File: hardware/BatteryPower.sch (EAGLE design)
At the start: 36 parts, among them U1 CH004-2032LF, U2 ACS711ELCTR-12AB-T, U3 ACS711ELCTR-12AB-T

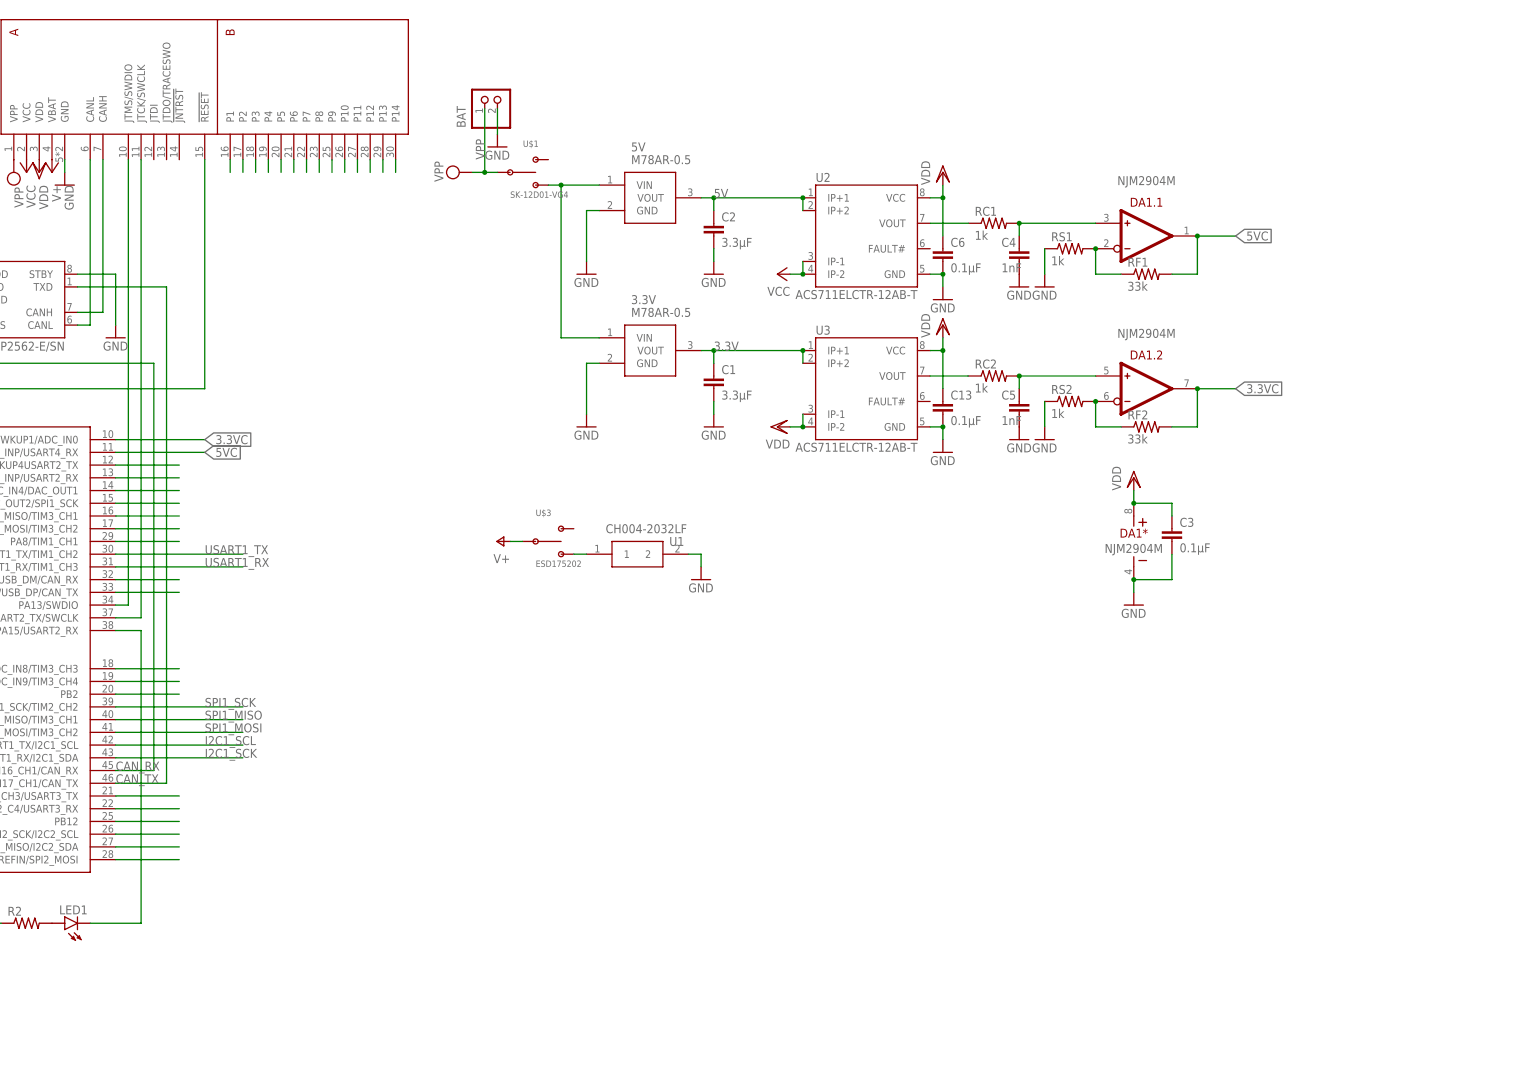
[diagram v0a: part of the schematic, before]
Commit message: Layout battery power board
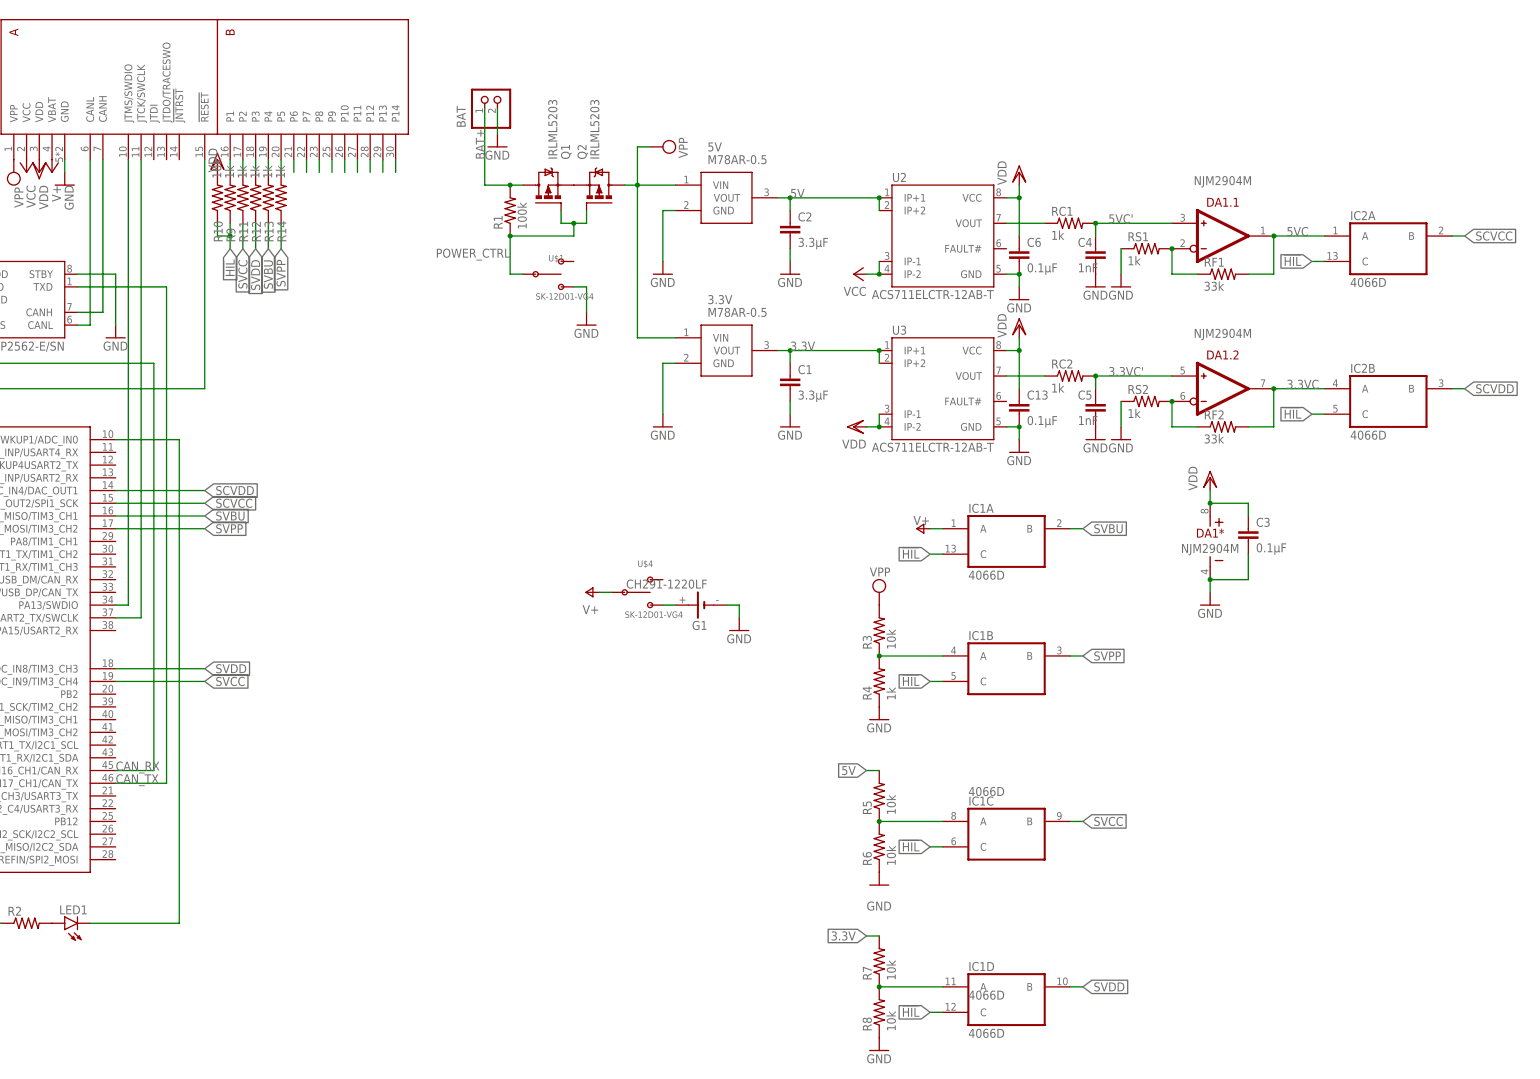
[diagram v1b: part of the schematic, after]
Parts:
- removed U$3: ESD175202, switches:ESD175202
- removed U1: CH004-2032LF, CH004-2032LF:CH004-2032LF
- added G1: CH291-1220LF, battery:CH291-1220LF
- added IC1, IC2: 4066D, 40xx:4066D
- added Q1, Q2: IRLML5203, transistor-power:IRLML5203
- added R1: 100k, rcl:R-US_R0603
- added R10, R3, R5, R6, R7, R8: 10k, rcl:R-US_R0603
- added R11, R12, R13, R14, R4, R9: 1k, rcl:R-US_R0603
- added U$4: SK-12D01-VG4, switches:SK-12D01-VG4
- BAT: device jst-ph:S2B-PH-K-S -> con-jst-xh:S2B-XH-A
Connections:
- net N$2 renamed 5VC'
- net N$3 renamed 3.3VC'
- removed net I2C1_SCK: STM32F001.PB7/USART1_RX/I2C1_SDA
- removed net I2C1_SCL: STM32F001.PB6USART1_TX/I2C1_SCL
- removed net N$11: U$3.B, U1.1
- removed net N$53: STM32F001.PA2/ADC_IN2/WKUP4USART2_TX
- removed net N$54: STM32F001.PA3/ADC_IN3/COMP2_INP/USART2_RX
- removed net N$55: STM32F001.PA4/ADC_IN4/DAC_OUT1
- removed net N$56: STM32F001.PA5/ADC_IN5/DAC_OUT2/SPI1_SCK
- removed net N$57: STM32F001.PA6/ADC_IN6/SPI1_MISO/TIM3_CH1
- removed net N$58: STM32F001.PA7/ADC_IN7/SPI1_MOSI/TIM3_CH2
- removed net N$59: STM32F001.PA8/TIM1_CH1
- removed net N$60: STM32F001.PA11/USB_DM/CAN_RX
- removed net N$61: STM32F001.PA12/USB_DP/CAN_TX
- removed net N$62: STM32F001.PB0/ADC_IN8/TIM3_CH3
- removed net N$63: STM32F001.PB1/ADC_IN9/TIM3_CH4
- removed net N$64: STM32F001.PB2
- removed net N$65: STM32F001.PB10/I2C2_SCL/TIM2_CH3/USART3_TX
- removed net N$66: STM32F001.PB11/I2C2_SDA/TIM2_C4/USART3_RX
- removed net N$67: STM32F001.PB12
- removed net N$68: STM32F001.PB13/SPI2_SCK/I2C2_SCL
- removed net N$69: STM32F001.PB14/SPI2_MISO/I2C2_SDA
- removed net N$70: STM32F001.PB15/WKUP7/RTC_REFIN/SPI2_MOSI
- removed net N$74: U$2.P1
- removed net SPI1_MISO: STM32F001.PB4/SPI1_MISO/TIM3_CH1
- removed net SPI1_MOSI: STM32F001.PB5/WKUP6/SPI1_MOSI/TIM3_CH2
- removed net SPI1_SCK: STM32F001.PB3/SPI1_SCK/TIM2_CH2
- removed net USART1_RX: STM32F001.PA10/USART1_RX/TIM1_CH3
- removed net USART1_TX: STM32F001.PA9/USART1_TX/TIM1_CH2
- new net !HIL!: IC1A.C, IC1B.C, IC1C.C, IC1D.C, IC2A.C, IC2B.C, R10.1, R9.1
- new net BAT+: BAT.1, Q1.D, R1.2
- new net BU+: G1.+, U$4.B
- new net N$2: Q1.S, Q2.S
- new net POWER_CTRL: Q1.G, Q2.G, R1.1, U$1.C
- new net PVCC: IC1C.A, R5.1, R6.2
- new net PVDD: IC1D.A, R7.1, R8.2
- new net PVPP: IC1B.A, R3.1, R4.2
- new net SCVCC: IC2A.B, STM32F001.PA5/ADC_IN5/DAC_OUT2/SPI1_SCK
- new net SCVDD: IC2B.B, STM32F001.PA4/ADC_IN4/DAC_OUT1
- new net SVBU: IC1A.B, R13.1, STM32F001.PA6/ADC_IN6/SPI1_MISO/TIM3_CH1
- new net SVCC: IC1C.B, R11.1, STM32F001.PB1/ADC_IN9/TIM3_CH4
- new net SVDD: IC1D.B, R12.1, STM32F001.PB0/ADC_IN8/TIM3_CH3
- new net SVPP: IC1B.B, R14.1, STM32F001.PA7/ADC_IN7/SPI1_MOSI/TIM3_CH2
- net 3.3V: now also R7.2
- net 3.3VC: now also IC2B.A; no longer STM32F001.PA0/USART4_TX/WKUP1/ADC_IN0
- net 5V: now also R5.2
- net 5VC: now also IC2A.A; no longer STM32F001.PA1/ADC_IN1/COMP1_INP/USART4_RX
- net GND: now also G1.-, R4.1, R6.1, R8.1, U$1.B; no longer U1.2
- net N$1: now also R9.2, U$2.P1; no longer 3.3V.VIN, 5V.VIN, U$1.B
- net N$48: now also R14.2
- net N$49: now also R13.2
- net N$50: now also R12.2
- net N$73: now also STM32F001.PA0/USART4_TX/WKUP1/ADC_IN0; no longer STM32F001.PA15/USART2_RX
- net N$75: now also R11.2
- net VBAT: now also IC1A.A, U$4.C; no longer U$3.C
- net VDD: now also R10.2
- net VPP: now also 3.3V.VIN, 5V.VIN, Q2.D, R3.2; no longer BAT.1, U$1.C
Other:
- moved on the sheet: 3.3V, 5V, C1, C13, C2, C3, C4, C5, C6, DA1*, DA1.1, DA1.2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

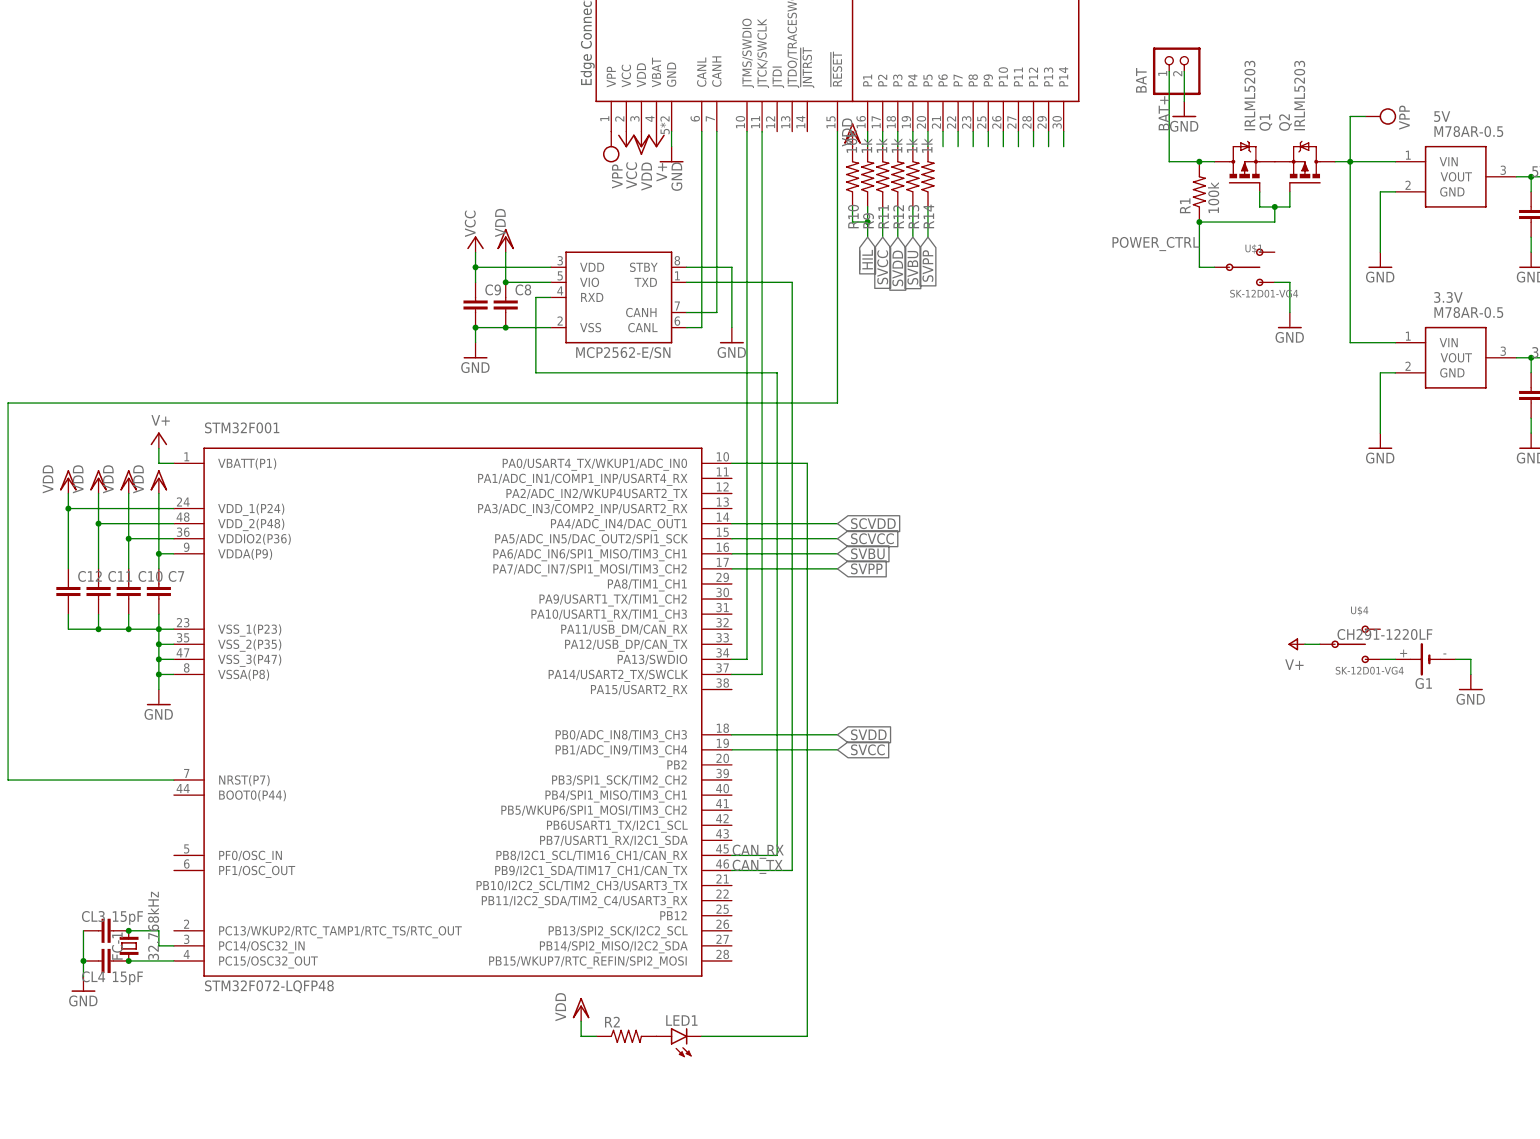
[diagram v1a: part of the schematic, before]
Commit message: Complete battery power board
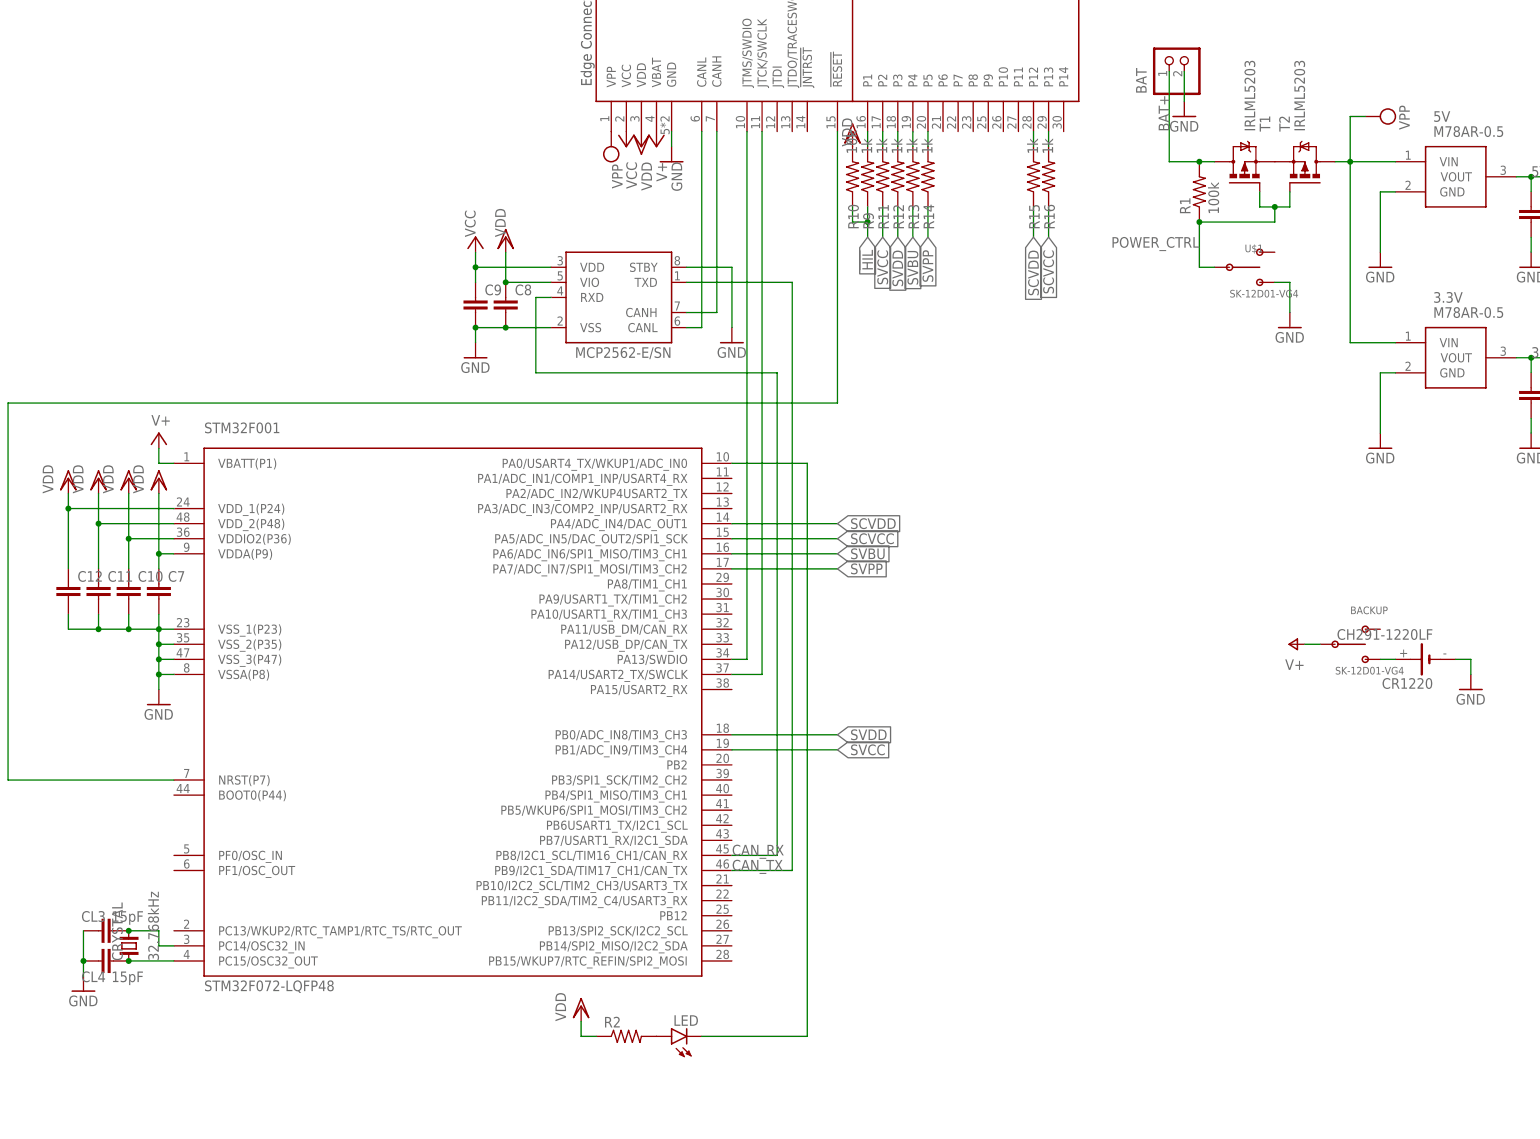
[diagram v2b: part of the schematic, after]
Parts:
- added R15, R16: 1k, resistor:R-US_R0603
- renumbered FC-1 to CRYSTAL, G1 to CR1220, LED1 to LED, MCP1 to MCP2562, Q1 to T1, Q2 to T2, U$4 to BACKUP
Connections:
- removed net N$33: U$2.P14
- removed net N$36: U$2.P11
- removed net N$43: U$2.P10
- removed net N$44: U$2.P9
- removed net N$45: U$2.P8
- removed net N$46: U$2.P7
- removed net N$47: U$2.P6
- net N$34: now also R16.2
- net N$35: now also R15.2
- net SCVCC: now also R16.1
- net SCVDD: now also R15.1
